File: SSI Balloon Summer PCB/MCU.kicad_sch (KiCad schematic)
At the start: 0 parts

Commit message: MCU sheet initial draft
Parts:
- added C24, C25, C26, C29: 100nF, symbol Device:C
- added C27, C28: 4.7uF, symbol Device:C
- added C30: 1uF, symbol Device:C
- added C31, C32: 8.2pF, symbol Device:C
- added C33: 0.1uF, symbol Device:C
- added J5: Conn_01x05, Connector_PinHeader_2.54mm:PinHeader_1x05_P2.54mm_Vertical, symbol Connector_Generic:Conn_01x05
- added R13: R_EXT, symbol Device:R
- added R14, R15: 10k, symbol Device:R
- added SW2, SW3: SW_SPST, symbol Switch:SW_SPST
- added U7: STM32F411CEUx, Package_DFN_QFN:QFN-48-1EP_7x7mm_P0.5mm_EP5.6x5.6mm, symbol MCU_ST_STM32F4:STM32F411CEUx
- added Y1: ABM8W-12.0000MHZ-8-K1Z-T3, ABM8W-12.0000MHZ-8-K1Z-T3:XTAL_ABM8W-12.0000MHZ-8-K1Z-T3, symbol ABM8W-12.0000MHZ-8-K1Z-T3:ABM8W-12.0000MHZ-8-K1Z-T3
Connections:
- new net: C27.1, U7.22 (VCAP1)
- new net: C32.2, R13.1, Y1.3
- new net +3.3V: C24.1, C25.1, C26.1, C28.1, C29.1, C30.1, J5.5 (Pin_5), R14.1, SW3.2 (B), U7.1 (VBAT), U7.24 (VDD), U7.36 (VDD), U7.48 (VDD), U7.9 (VDDA)
- new net APRS_RX: U7.13 (PA3)
- new net APRS_TX: U7.12 (PA2)
- new net BOOT0: R15.1, SW3.1 (A), U7.44 (BOOT0)
- new net GND: C24.2, C25.2, C26.2, C27.2, C28.2, C29.2, C30.2, C31.1, C32.1, C33.2, J5.1 (Pin_1), R15.2, SW2.1 (A), U7.23 (VSS), U7.35 (VSS), U7.47 (VSS), U7.49 (VSS), U7.8 (VSSA), Y1.2 (GND), Y1.4 (GND)
- new net GPS_RX: U7.31 (PA10)
- new net GPS_TX: U7.30 (PA9)
- new net MISO: U7.16 (PA6)
- new net MOSI: U7.17 (PA7)
- new net NRST: C33.1, J5.2 (Pin_2), R14.2, SW2.2 (B), U7.7 (NRST)
- new net OSC_IN: C31.2, U7.5 (PH0), Y1.1
- new net OSC_OUT: R13.2, U7.6 (PH1)
- new net PI_ZERO_RX: U7.33 (PA12)
- new net PI_ZERO_TX: U7.32 (PA11)
- new net SCK: U7.15 (PA5)
- new net SCL: U7.42 (PB6)
- new net SDA: U7.43 (PB7)
- new net SWCLK: J5.3 (Pin_3), U7.37 (PA14)
- new net SWDIO: J5.4 (Pin_4), U7.34 (PA13)
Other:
- note added: "BOOT0 (button forces it high)"
- note added: "Both 100nF and 1uF for VDDA"
- note added: "Bulk decoupling cap goes to one of the VDD"
- note added: "Communication Protocols Legend SPI: SCK, MISO, MOSI, (CS will be GPIO) I2C: SCL, SDA UART: APRS_RX/TX, GPS_RX/TX, PI_ZERO_RX/TX"
- note added: "Each VDD needs a decoupling cap, as close as possible to the pin"
- note added: "NRST (button forces it low)"
- note added: "R_EXT value TBD; will try 0R at first"
- note added: "Serial Wire Flash/Debug (STLink needed!)"

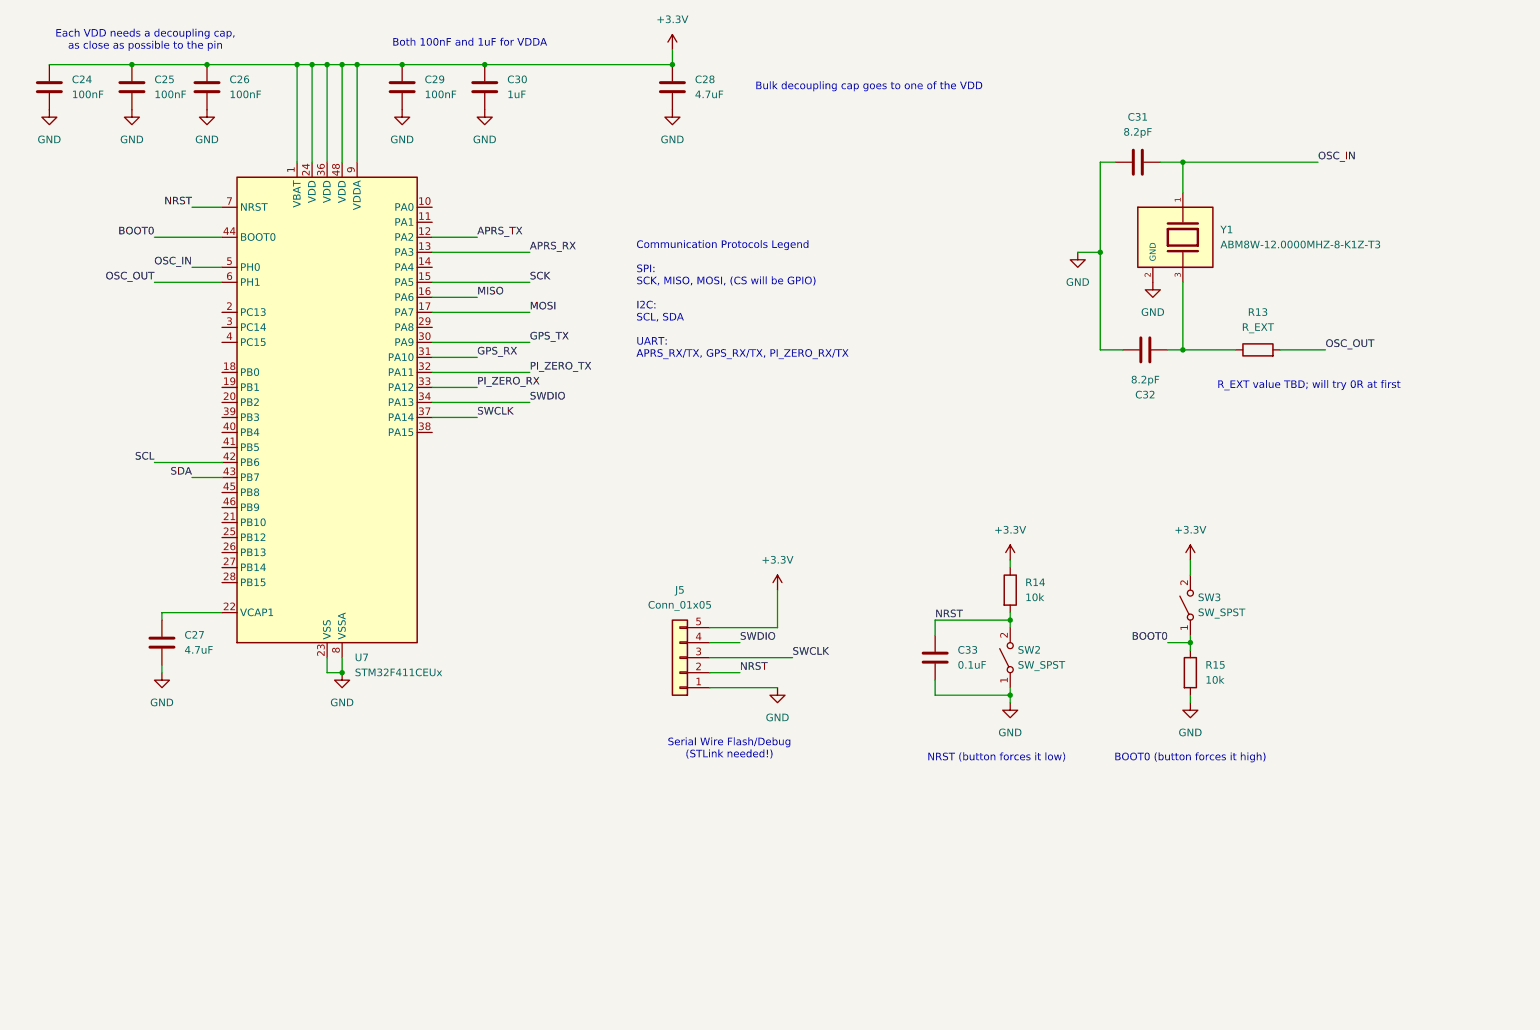
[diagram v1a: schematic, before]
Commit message: Added CS pins for SPI and hierarchical labels to MCU sheet
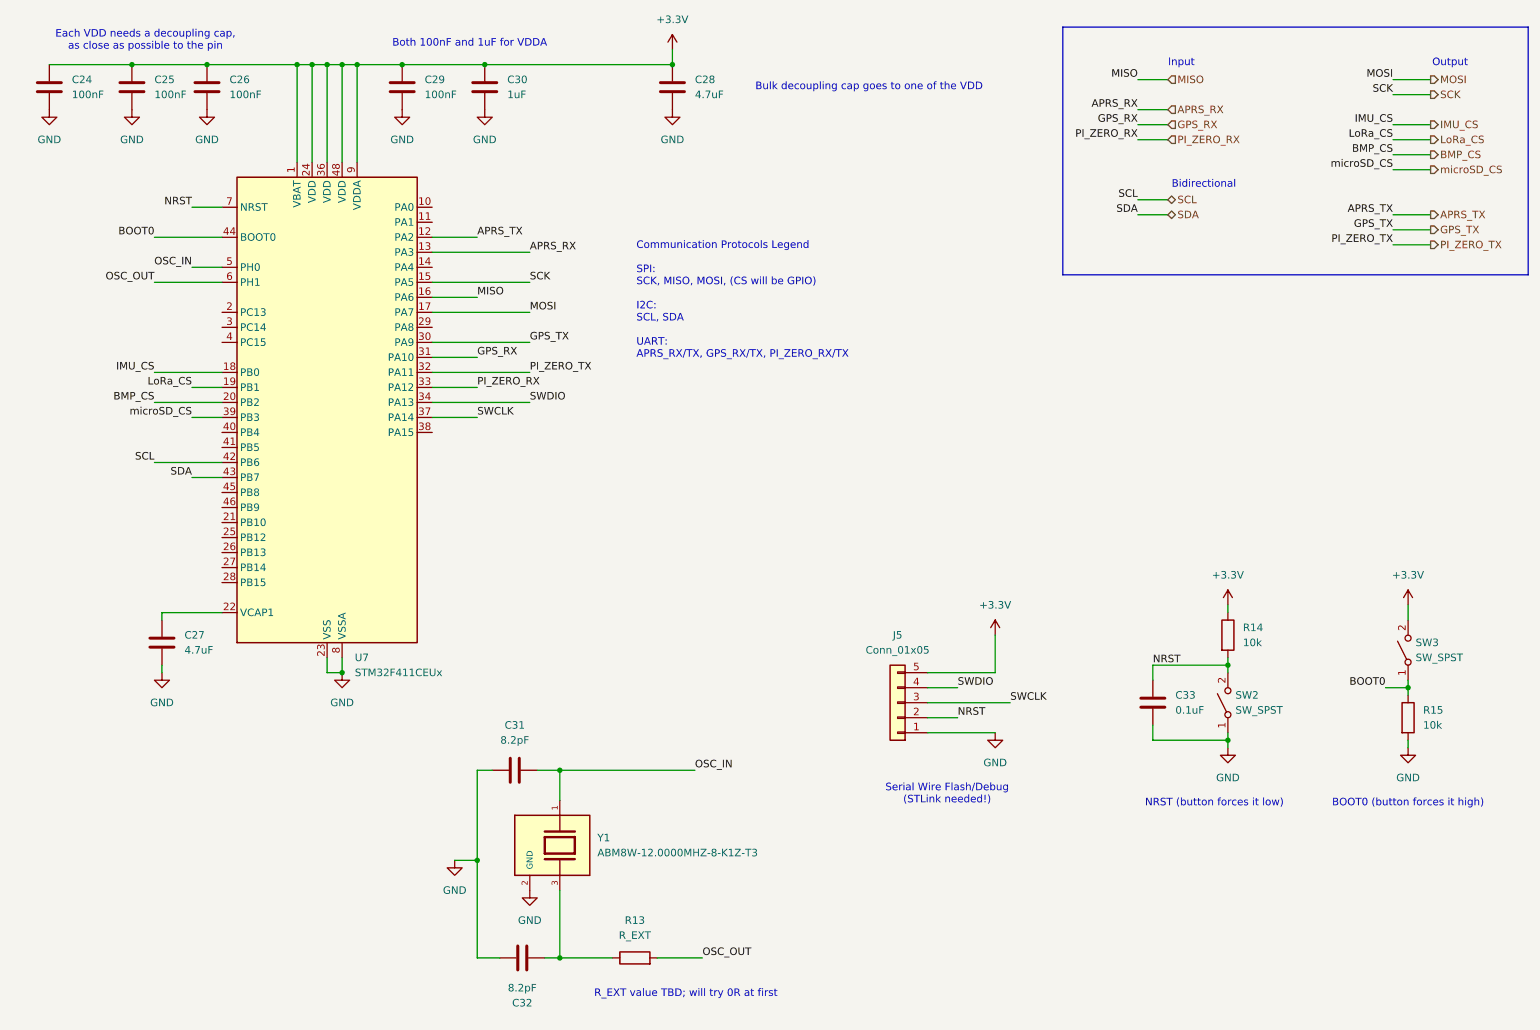
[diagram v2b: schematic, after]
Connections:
- net IMU_CS: now reaches U7.18 (PB0)
- net LoRa_CS: now reaches U7.19 (PB1)
- net BMP_CS: now reaches U7.20 (PB2)
- net microSD_CS: now reaches U7.39 (PB3)
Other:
- note added: "Bidirectional"
- note added: "Input"
- note added: "Output"
- moved on the sheet: C31, C32, C33, J5, R13, R14, R15, SW2, SW3, Y1

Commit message: Standardized power symbols, added microSD sheet, and standardized hierarchical labels
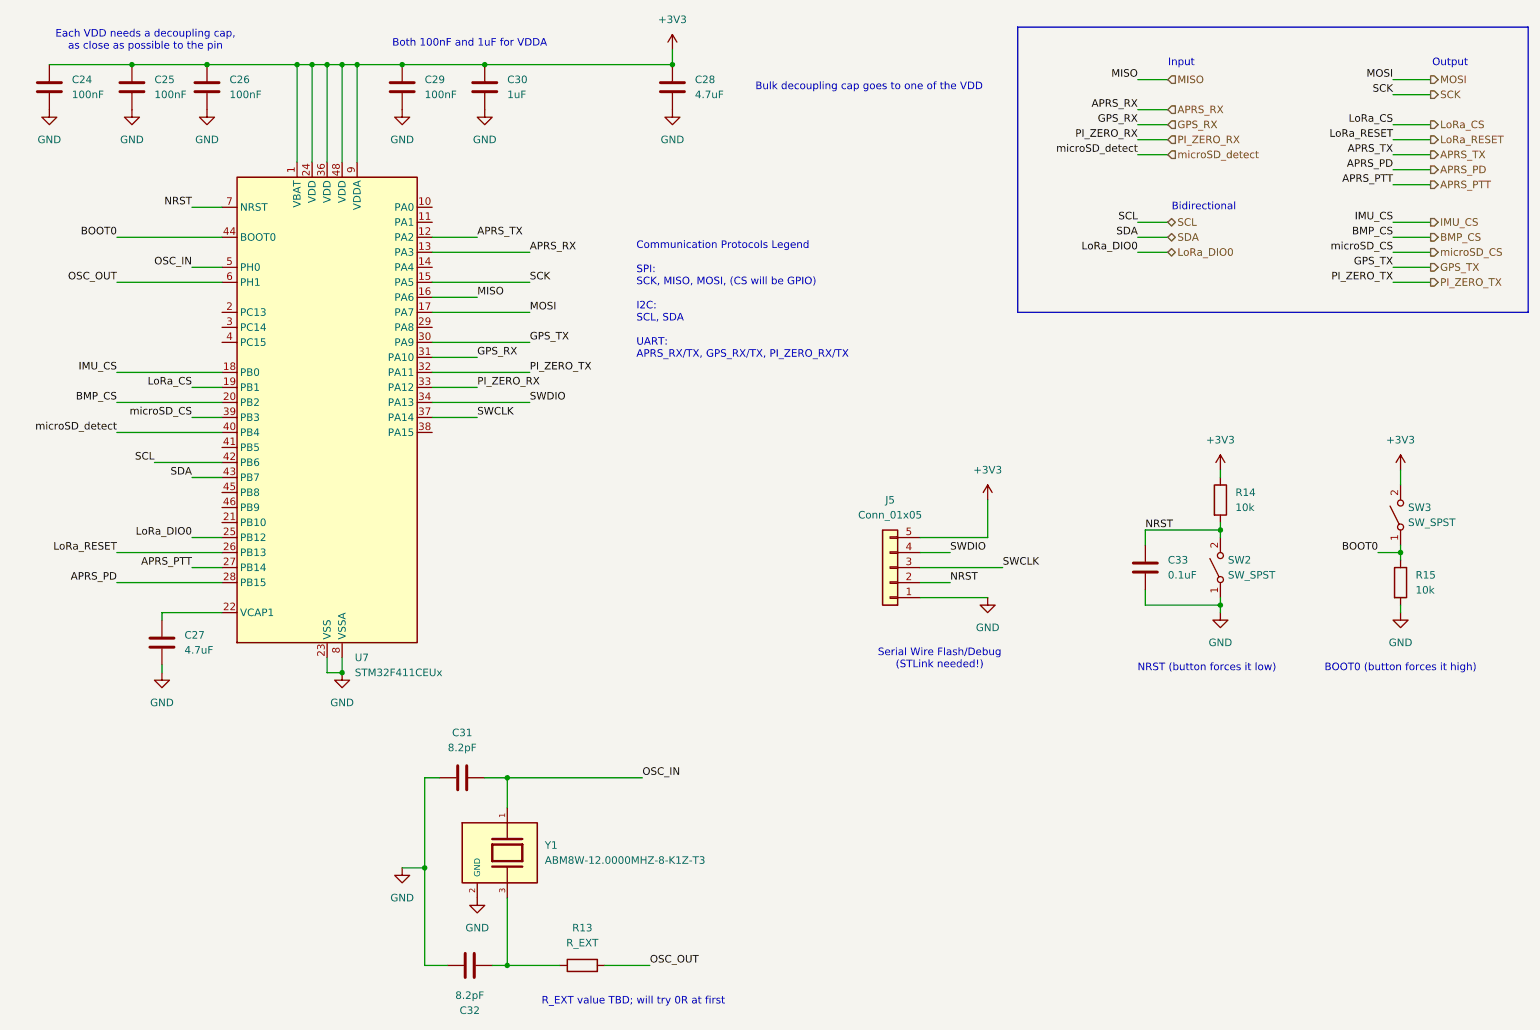
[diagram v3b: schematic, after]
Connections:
- net LoRa_DIO0: now reaches U7.25 (PB12)
- net LoRa_RESET: now reaches U7.26 (PB13)
- net APRS_PTT: now reaches U7.27 (PB14)
- net APRS_PD: now reaches U7.28 (PB15)
- net microSD_detect: now reaches U7.40 (PB4)
- net +3.3V renamed +3V3
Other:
- moved on the sheet: C31, C32, C33, J5, R13, R14, R15, SW2, SW3, Y1

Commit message: schematic
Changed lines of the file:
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@@
+	(wire
+		(pts
+			(xy 210.82 44.45) (xy 215.9 44.45)
+		)
+		(stroke
+			(width 0)
+			(type default)
+		)
+	)
 	(wire
 		(pts
@@
 		)
 	)
+	(label "+3V3"
+		(at 210.82 44.45 180)
+		(effects
+			(font
+				(size 1.27 1.27)
+			)
+			(justify right bottom)
+		)
+	)
 	(label "SCL"
 		(at 44.45 93.98 180)
@@
 		(effects
 			(font
+				(size 1.27 1.27)
+			)
+			(justify left)
+		)
+	)
+	(hierarchical_label "+3V3"
+		(shape input)
+		(at 215.9 44.45 0)
+		(effects
+			(font

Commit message: Finished GPS
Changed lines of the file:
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@@
 	(wire
 		(pts
-			(xy 254 41.91) (xy 260.35 41.91)
+			(xy 209.55 34.29) (xy 215.9 34.29)
 		)
 		(stroke
@@
 	(wire
 		(pts
-			(xy 210.82 36.83) (xy 215.9 36.83)
+			(xy 255.27 60.96) (xy 260.35 60.96)
 		)
 		(stroke
@@
 	(wire
 		(pts
-			(xy 254 60.96) (xy 260.35 60.96)
-		)
-		(stroke
-			(width 0)
-			(type default)
-		)
-	)
-	(wire
-		(pts
-			(xy 210.82 34.29) (xy 215.9 34.29)
+			(xy 209.55 36.83) (xy 215.9 36.83)
+		)
+		(stroke
+			(width 0)
+			(type default)
+		)
+	)
+	(wire
+		(pts
+			(xy 254 41.91) (xy 259.08 41.91)
 		)
 		(stroke
@@
 	)
 	(label "GPS_RX"
-		(at 210.82 36.83 180)
+		(at 255.27 60.96 180)
 		(effects
 			(font
@@
 	)
 	(label "GPS_TX"
-		(at 254 60.96 180)
+		(at 209.55 36.83 180)
 		(effects
 			(font
@@
 	)
 	(label "APRS_RX"
-		(at 210.82 34.29 180)
+		(at 254 41.91 180)
 		(effects
 			(font
@@
 	)
 	(label "APRS_TX"
-		(at 254 41.91 180)
+		(at 209.55 34.29 180)
 		(effects
 			(font
@@
 	)
 	(hierarchical_label "APRS_RX"
-		(shape input)
-		(at 215.9 34.29 0)
+		(shape output)
+		(at 259.08 41.91 0)
 		(effects
 			(font
@@
 	)
 	(hierarchical_label "GPS_RX"
-		(shape input)
-		(at 215.9 36.83 0)
+		(shape output)
+		(at 260.35 60.96 0)
 		(effects
 			(font
@@
 	)
 	(hierarchical_label "GPS_TX"
-		(shape output)
-		(at 260.35 60.96 0)
+		(shape input)
+		(at 215.9 36.83 0)
 		(effects
 			(font
@@
 	)
 	(hierarchical_label "APRS_TX"
-		(shape output)
-		(at 260.35 41.91 0)
-		(effects
-			(font
+		(shape input)
+		(at 215.9 34.29 0)
+		(effects
+			(font

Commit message: adding IMU footprint+symbol
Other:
- note added: "Passive"
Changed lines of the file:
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@@
+		)
+	)
+	(text "Passive"
+		(exclude_from_sim no)
+		(at 218.44 62.738 0)
+		(effects
+			(font
+				(size 1.27 1.27)
+			)
 		)
 	)
@@
 	(wire
 		(pts
+			(xy 209.55 66.04) (xy 218.44 66.04)
+		)
+		(stroke
+			(width 0)
+			(type default)
+		)
+	)
+	(wire
+		(pts
 			(xy 76.2 127) (xy 76.2 129.54)
 		)
@@
 			)
 			(justify right bottom)
+		)
+	)
+	(label "GND"
+		(at 209.55 66.04 0)
+		(effects
+			(font
+				(size 1.27 1.27)
+			)
+			(justify left bottom)
 		)
 	)
@@
 		(effects
 			(font
+				(size 1.27 1.27)
+			)
+			(justify left)
+		)
+	)
+	(hierarchical_label "GND"
+		(shape passive)
+		(at 218.44 66.04 0)
+		(effects
+			(font
